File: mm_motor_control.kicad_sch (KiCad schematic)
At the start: 0 parts

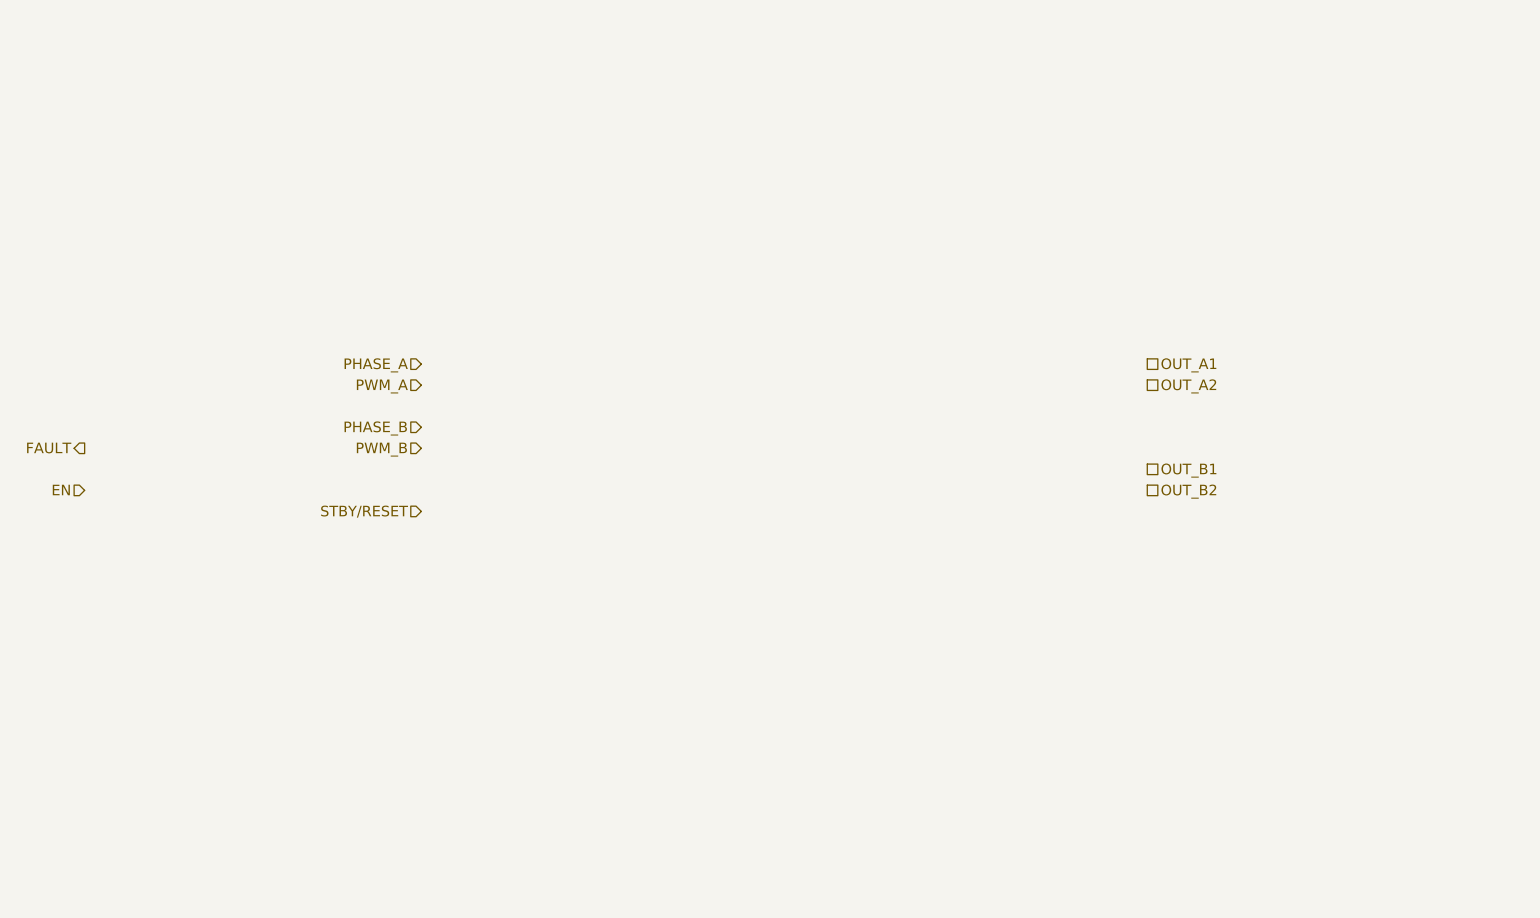
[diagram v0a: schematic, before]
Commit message: ended PCB + added reverse voltage protection
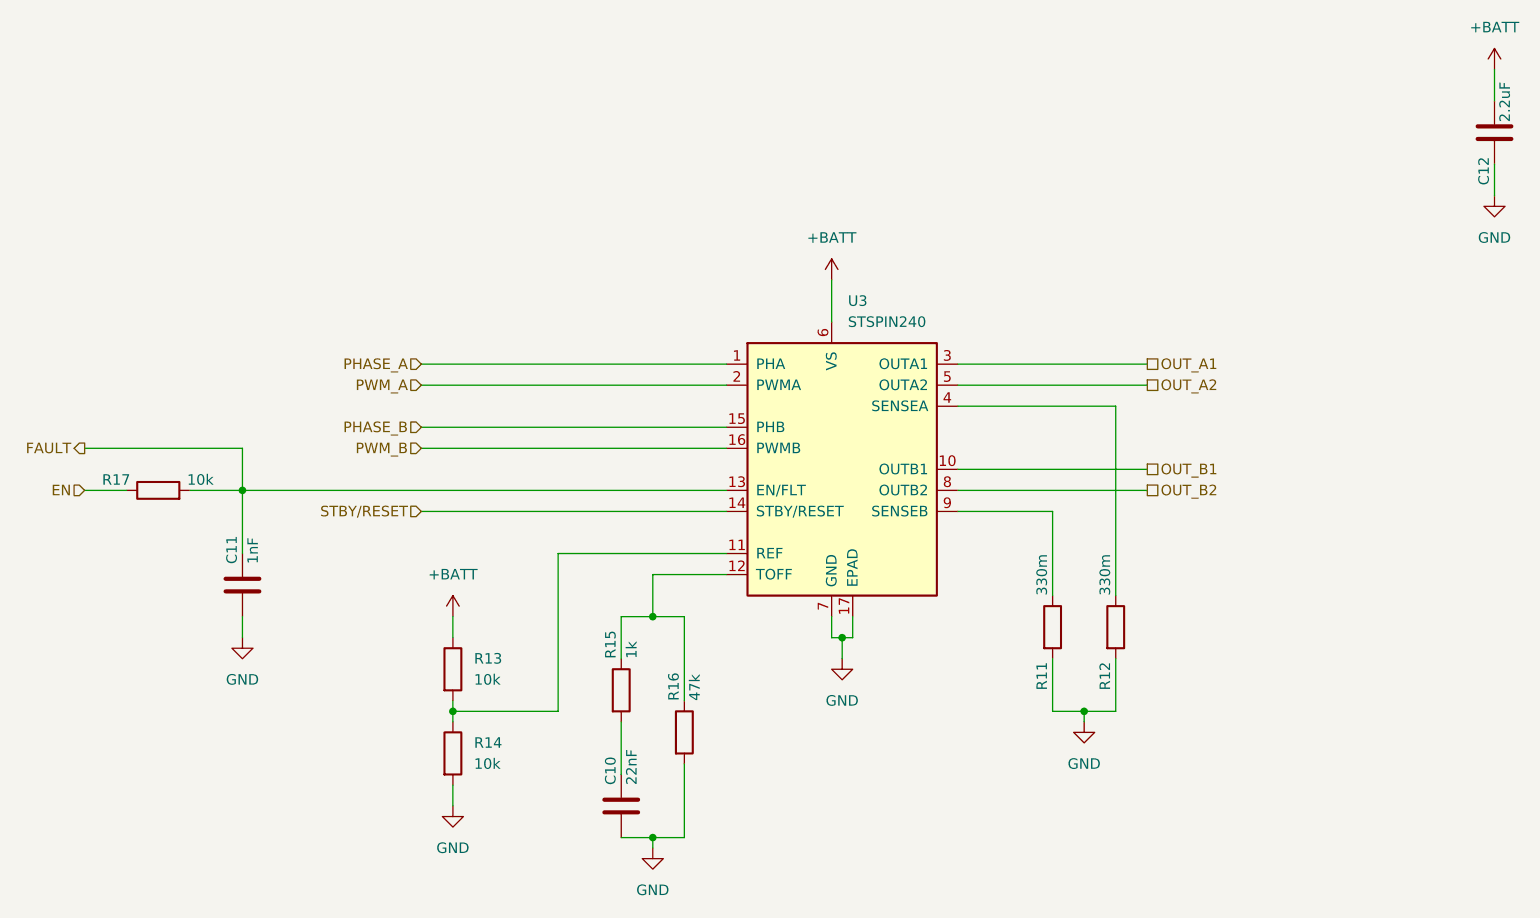
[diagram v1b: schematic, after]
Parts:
- added C10: 22nF, Capacitor_SMD:C_0603_1608Metric, symbol Device:C
- added C11: 1nF, Capacitor_SMD:C_0603_1608Metric, symbol Device:C
- added C12: 2.2uF, Capacitor_SMD:C_0603_1608Metric, symbol Device:C
- added R11, R12: 330m, Resistor_SMD:R_2512_6332Metric, symbol Device:R
- added R13, R14, R17: 10k, Resistor_SMD:R_0603_1608Metric, symbol Device:R
- added R15: 1k, Resistor_SMD:R_0603_1608Metric, symbol Device:R
- added R16: 47k, Resistor_SMD:R_0603_1608Metric, symbol Device:R
- added U3: STSPIN240, Package_DFN_QFN:VQFN-16-1EP_3x3mm_P0.5mm_EP1.8x1.8mm, symbol Driver_Motor:STSPIN240
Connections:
- net EN: now also R17.1
- net FAULT: now also C11.1, R17.2, U3.13 (EN/FLT)
- net OUT_A1: now also U3.3 (OUTA1)
- net OUT_A2: now also U3.5 (OUTA2)
- net OUT_B1: now also U3.10 (OUTB1)
- net OUT_B2: now also U3.8 (OUTB2)
- net PHASE_A: now also U3.1 (PHA)
- net PHASE_B: now also U3.15 (PHB)
- net PWM_A: now also U3.2 (PWMA)
- net PWM_B: now also U3.16 (PWMB)
- net STBY/RESET: now also U3.14 (STBY/RESET)
- new net: R11.1, U3.9 (SENSEB)
- new net: R15.1, R16.1, U3.12 (TOFF)
- new net: R13.2, R14.1, U3.11 (REF)
- new net: R12.1, U3.4 (SENSEA)
- new net: C10.1, R15.2
- new net +BATT: C12.1, R13.1, U3.6 (VS)
- new net GND: C10.2, C11.2, C12.2, R11.2, R12.2, R14.2, R16.2, U3.17 (EPAD), U3.7 (GND)
